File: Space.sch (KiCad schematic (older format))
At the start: 0 parts

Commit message: Replace MCU, route bus
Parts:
- added D66, D67, D68: D_Small, Diodes_SMD:D_SOD-123, symbol D_Small
- added SP1, SP7: MX-2.25U, MX_Alps_Hybrid:MX-2.25U-ReversedStabilizers, symbol MX-2.25U
- added SP2: MX-7U, MX_Alps_Hybrid:MX-7U-ReversedStabilizers, symbol MX-7U
- added SP3: MX-6.25U, MX_Alps_Hybrid:MX-6.25U-ReversedStabilizers, symbol MX-7U
- added SP4: MX-1.25U, MX_Alps_Hybrid:MX-1.25U, symbol MX-7U
- added SP5, SP9: MX-2.75U, MX_Alps_Hybrid:MX-2.75U-ReversedStabilizers, symbol MX-2.25U
- added SP6: MX-6.5U, MX_Alps_Hybrid:MX-6.5U-ReversedStabilizers, symbol MX-7U
- added SP8: MX-1.5U, MX_Alps_Hybrid:MX-1.5U, symbol MX-7U
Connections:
- new net: D67.2 (A), SP2.2 (ROW)
- new net: D66.2 (A), SP1.2 (ROW)
- new net: D68.2 (A), SP5.2 (ROW)
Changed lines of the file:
@@
 $Descr A4 11693 8268
 encoding utf-8
-Sheet 1 6
+Sheet 5 6
 Title ""
 Date ""
@@
 Comment4 ""
 $EndDescr
+$Comp
+L MX-7U SP2
+U 1 1 5ACDBE00
+P 2225 1550
+F 0 "SP2" H 2225 1675 60  0000 C CNN
+F 1 "MX-7U" H 2225 1600 20  0000 C CNN
+F 2 "MX_Alps_Hybrid:MX-7U-ReversedStabilizers" H 2200 1525 60  0001 C CNN
+F 3 "" H 2200 1525 60  0001 C CNN
+	1    2225 1550
+	1    0    0    -1
+$EndComp
+$Comp
+L MX-2.25U SP1
+U 1 1 5ACDBE1D
+P 1525 1550
+F 0 "SP1" H 1525 1675 60  0000 C CNN
+F 1 "MX-2.25U" H 1525 1600 20  0000 C CNN
+F 2 "MX_Alps_Hybrid:MX-2.25U-ReversedStabilizers" H 1500 1525 60  0001 C CNN
+F 3 "" H 1500 1525 60  0001 C CNN
+	1    1525 1550
+	1    0    0    -1
+$EndComp
+$Comp
+L MX-2.25U SP7
+U 1 1 5ACDBE8E
+P 1525 2250
+F 0 "SP7" H 1525 2375 60  0000 C CNN
+F 1 "MX-2.25U" H 1525 2300 20  0000 C CNN
+F 2 "MX_Alps_Hybrid:MX-2.25U-ReversedStabilizers" H 1500 2225 60  0001 C CNN
+F 3 "" H 1500 2225 60  0001 C CNN
+	1    1525 2250
+	1    0    0    -1
+$EndComp
+$Comp
+L D_Small D66
+U 1 1 5ACDBEFA
+P 1425 1825
+F 0 "D66" H 1375 1905 50  0000 L CNN
+F 1 "D_Small" H 1275 1745 50  0000 L CNN
+F 2 "Diodes_SMD:D_SOD-123" V 1425 1825 50  0001 C CNN
+F 3 "" V 1425 1825 50  0001 C CNN
+	1    1425 1825
+	0    -1   -1   0
+$EndComp
+Wire Wire Line
+	1425 1725 1500 1725
+$Comp
+L D_Small D67
+U 1 1 5ACDC3D9
+P 2125 1825
+F 0 "D67" H 2075 1905 50  0000 L CNN
+F 1 "D_Small" H 1975 1745 50  0000 L CNN
+F 2 "Diodes_SMD:D_SOD-123" V 2125 1825 50  0001 C CNN
+F 3 "" V 2125 1825 50  0001 C CNN
+	1    2125 1825
+	0    -1   -1   0
+$EndComp
+Wire Wire Line
+	2125 1725 2200 1725
+$Comp
+L MX-7U SP4
+U 1 1 5ACDC6A9
+P 2225 2250
+F 0 "SP4" H 2225 2375 60  0000 C CNN
+F 1 "MX-1.25U" H 2225 2300 20  0000 C CNN
+F 2 "MX_Alps_Hybrid:MX-1.25U" H 2200 2225 60  0001 C CNN
+F 3 "" H 2200 2225 60  0001 C CNN
+	1    2225 2250
+	1    0    0    -1
+$EndComp
+$Comp
+L MX-7U SP6
+U 1 1 5ACDCCED
+P 2225 2850
+F 0 "SP6" H 2225 2975 60  0000 C CNN
+F 1 "MX-6.5U" H 2225 2900 20  0000 C CNN
+F 2 "MX_Alps_Hybrid:MX-6.5U-ReversedStabilizers" H 2200 2825 60  0001 C CNN
+F 3 "" H 2200 2825 60  0001 C CNN
+	1    2225 2850
+	1    0    0    -1
+$EndComp
+$Comp
+L MX-7U SP8
+U 1 1 5ACDCFF5
+P 2225 3500
+F 0 "SP8" H 2225 3625 60  0000 C CNN
+F 1 "MX-1.5U" H 2225 3550 20  0000 C CNN
+F 2 "MX_Alps_Hybrid:MX-1.5U" H 2200 3475 60  0001 C CNN
+F 3 "" H 2200 3475 60  0001 C CNN
+	1    2225 3500
+	1    0    0    -1
+$EndComp
+$Comp
+L MX-2.25U SP5
+U 1 1 5ACDD407
+P 2900 1550
+F 0 "SP5" H 2900 1675 60  0000 C CNN
+F 1 "MX-2.75U" H 2900 1600 20  0000 C CNN
+F 2 "MX_Alps_Hybrid:MX-2.75U-ReversedStabilizers" H 2875 1525 60  0001 C CNN
+F 3 "" H 2875 1525 60  0001 C CNN
+	1    2900 1550
+	1    0    0    -1
+$EndComp
+$Comp
+L MX-2.25U SP9
+U 1 1 5ACDD40D
+P 2900 2250
+F 0 "SP9" H 2900 2375 60  0000 C CNN
+F 1 "MX-2.75U" H 2900 2300 20  0000 C CNN
+F 2 "MX_Alps_Hybrid:MX-2.75U-ReversedStabilizers" H 2875 2225 60  0001 C CNN
+F 3 "" H 2875 2225 60  0001 C CNN
+	1    2900 2250
+	1    0    0    -1
+$EndComp
+$Comp
+L D_Small D68
+U 1 1 5ACDD413
+P 2800 1825
+F 0 "D68" H 2750 1905 50  0000 L CNN
+F 1 "D_Small" H 2650 1745 50  0000 L CNN
+F 2 "Diodes_SMD:D_SOD-123" V 2800 1825 50  0001 C CNN
+F 3 "" V 2800 1825 50  0001 C CNN
+	1    2800 1825
+	0    -1   -1   0
+$EndComp
+Wire Wire Line
+	2800 1725 2875 1725
+$Comp
+L MX-7U SP3
+U 1 1 5ACDE3EF
+P 2225 4275
+F 0 "SP3" H 2225 4400 60  0000 C CNN
+F 1 "MX-6.25U" H 2225 4325 20  0000 C CNN
+F 2 "MX_Alps_Hybrid:MX-6.25U-ReversedStabilizers" H 2200 4250 60  0001 C CNN
+F 3 "" H 2200 4250 60  0001 C CNN
+	1    2225 4275
+	1    0    0    -1
+$EndComp
 $EndSCHEMATC

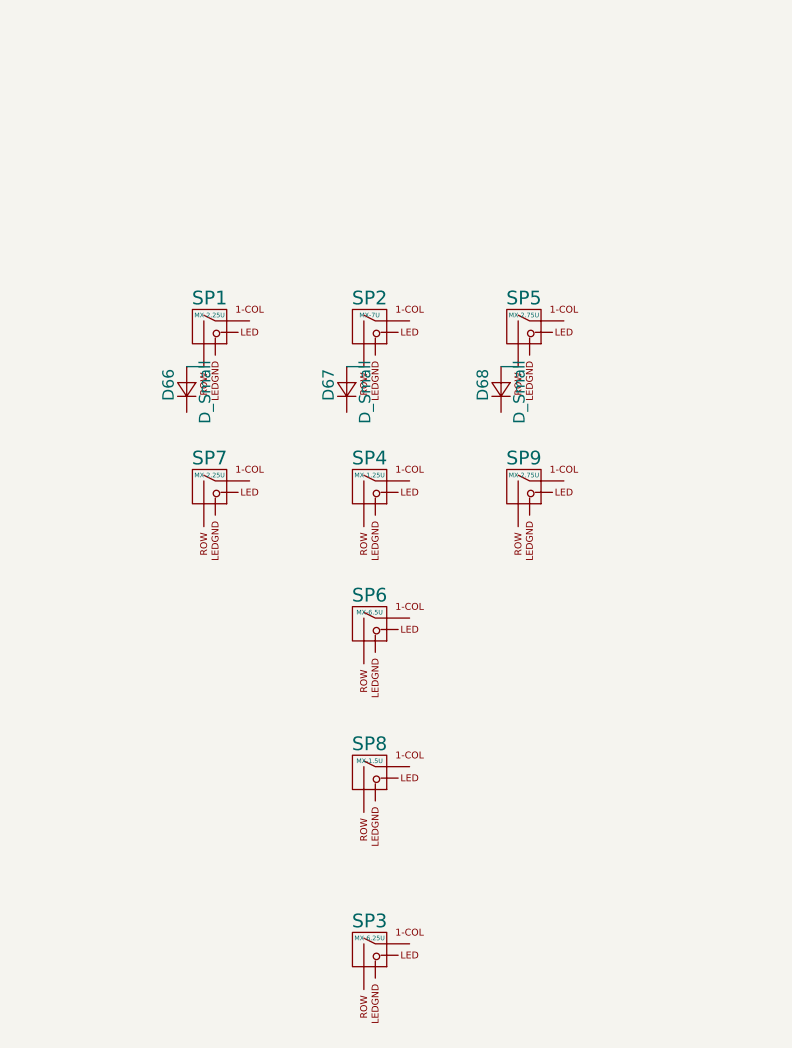
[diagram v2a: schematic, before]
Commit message: Finish project basic routing
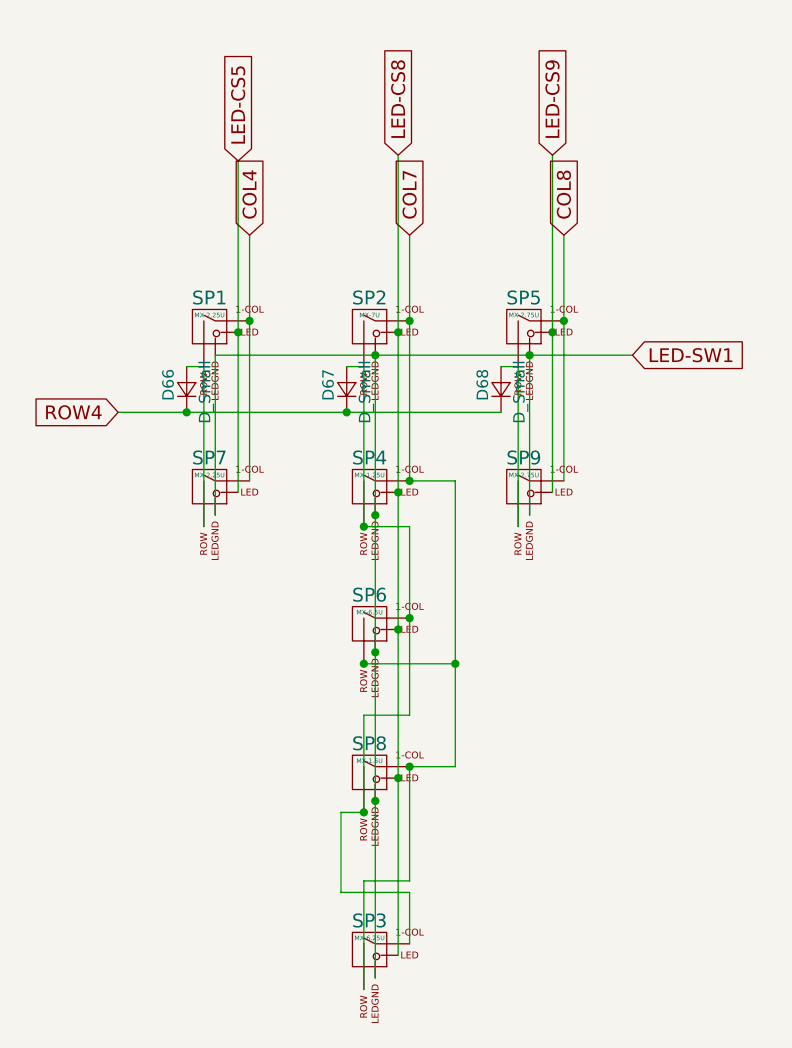
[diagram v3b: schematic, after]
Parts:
- SP4: footprint MX_Alps_Hybrid:MX-1.25U -> MX_Alps_Hybrid:MX-1.25U-FLIPPED
- SP6: footprint MX_Alps_Hybrid:MX-6.5U-ReversedStabilizers -> MX_Alps_Hybrid:MX-6.5U-FLIPPED-ReversedStabilizers
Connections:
- net COL7: now reaches SP2.1 (COL)
- net COL7: now also SP3.2 (ROW), SP4.1 (COL), SP6.2 (ROW), SP8.1 (COL)
- net at D67.2 (A), SP2.2 (ROW): now also SP3.1 (COL), SP4.2 (ROW), SP6.1 (COL), SP8.2 (ROW)
- net LED-CS8: now reaches SP2.3 (LED)
- net LED-CS8: now also SP3.3 (LED), SP4.3 (LED), SP6.3 (LED), SP8.3 (LED)
- net LED-SW1: now reaches SP2.4 (LEDGND)
- net LED-SW1: now also SP1.4 (LEDGND), SP3.4 (LEDGND), SP4.4 (LEDGND), SP5.4 (LEDGND), SP6.4 (LEDGND), SP7.4 (LEDGND), SP8.4 (LEDGND), SP9.4 (LEDGND)
- net COL4: now reaches SP1.1 (COL)
- net COL4: now also SP7.1 (COL)
- net at D66.2 (A), SP1.2 (ROW): now also SP7.2 (ROW)
- net LED-CS5: now reaches SP1.3 (LED)
- net LED-CS5: now also SP7.3 (LED)
- net ROW4: now reaches D66.1 (K)
- net ROW4: now also D67.1 (K), D68.1 (K)
- net COL8: now reaches SP5.1 (COL)
- net COL8: now also SP9.1 (COL)
- net at D68.2 (A), SP5.2 (ROW): now also SP9.2 (ROW)
- net LED-CS9: now reaches SP5.3 (LED)
- net LED-CS9: now also SP9.3 (LED)
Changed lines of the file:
@@
 F 0 "SP4" H 2225 2375 60  0000 C CNN
 F 1 "MX-1.25U" H 2225 2300 20  0000 C CNN
-F 2 "MX_Alps_Hybrid:MX-1.25U" H 2200 2225 60  0001 C CNN
+F 2 "MX_Alps_Hybrid:MX-1.25U-FLIPPED" H 2200 2225 60  0001 C CNN
 F 3 "" H 2200 2225 60  0001 C CNN
 	1    2225 2250
@@
 F 0 "SP6" H 2225 2975 60  0000 C CNN
 F 1 "MX-6.5U" H 2225 2900 20  0000 C CNN
-F 2 "MX_Alps_Hybrid:MX-6.5U-ReversedStabilizers" H 2200 2825 60  0001 C CNN
+F 2 "MX_Alps_Hybrid:MX-6.5U-FLIPPED-ReversedStabilizers" H 2200 2825 60  0001 C CNN
 F 3 "" H 2200 2825 60  0001 C CNN
 	1    2225 2850
-	1    0    0    -1
-$EndComp
-$Comp
-L MX-7U SP8
-U 1 1 5ACDCFF5
-P 2225 3500
-F 0 "SP8" H 2225 3625 60  0000 C CNN
-F 1 "MX-1.5U" H 2225 3550 20  0000 C CNN
-F 2 "MX_Alps_Hybrid:MX-1.5U" H 2200 3475 60  0001 C CNN
-F 3 "" H 2200 3475 60  0001 C CNN
-	1    2225 3500
 	1    0    0    -1
 $EndComp
@@
 	1    0    0    -1
 $EndComp
+Wire Wire Line
+	1700 1150 1700 2225
+Wire Wire Line
+	1500 1725 1500 2425
+Connection ~ 1700 1525
+Wire Wire Line
+	2400 1150 2400 2225
+Wire Wire Line
+	2400 2425 2400 3250
+Wire Wire Line
+	2400 3475 2400 3975
+Connection ~ 2400 1525
+Connection ~ 2400 2225
+Wire Wire Line
+	2200 1725 2200 2425
+Connection ~ 2200 2425
+Connection ~ 2400 2825
+Connection ~ 2200 3675
+Wire Wire Line
+	3075 1150 3075 2225
+Wire Wire Line
+	2875 1725 2875 2425
+Wire Wire Line
+	1125 1925 2800 1925
+Connection ~ 2125 1925
+Connection ~ 1425 1925
+Text GLabel 1125 1925 0    60   Input ~ 0
+ROW4
+$Comp
+L MX-7U SP8
+U 1 1 5ACDCFF5
+P 2225 3500
+F 0 "SP8" H 2225 3625 60  0000 C CNN
+F 1 "MX-1.5U" H 2225 3550 20  0000 C CNN
+F 2 "MX_Alps_Hybrid:MX-1.5U" H 2200 3475 60  0001 C CNN
+F 3 "" H 2200 3475 60  0001 C CNN
+	1    2225 3500
+	1    0    0    -1
+$EndComp
+Wire Wire Line
+	2400 3975 2200 3975
+Wire Wire Line
+	2200 3975 2200 4450
+Wire Wire Line
+	2400 4250 2400 4025
+Wire Wire Line
+	2400 4025 2100 4025
+Wire Wire Line
+	2100 4025 2100 3675
+Wire Wire Line
+	2100 3675 2200 3675
+Connection ~ 2200 3025
+Connection ~ 2400 3475
+Wire Wire Line
+	2400 2225 2600 2225
+Wire Wire Line
+	2600 2225 2600 3475
+Wire Wire Line
+	2600 3025 2200 3025
+Wire Wire Line
+	2200 2425 2400 2425
+Wire Wire Line
+	2400 3250 2200 3250
+Wire Wire Line
+	2200 3250 2200 3675
+Wire Wire Line
+	2600 3475 2400 3475
+Connection ~ 2600 3025
+Connection ~ 3075 1525
+Text GLabel 3075 1150 1    60   Input ~ 0
+COL8
+Text GLabel 2400 1150 1    60   Input ~ 0
+COL7
+Text GLabel 1700 1150 1    60   Input ~ 0
+COL4
+Wire Wire Line
+	1650 825  1650 2275
+Connection ~ 1650 1575
+Text GLabel 1650 825  1    60   Input ~ 0
+LED-CS5
+Wire Wire Line
+	2350 800  2350 4300
+Connection ~ 2350 2275
+Connection ~ 2350 1575
+Text GLabel 2350 800  1    60   Input ~ 0
+LED-CS8
+Wire Wire Line
+	3025 800  3025 2275
+Connection ~ 3025 1575
+Connection ~ 2350 2875
+Connection ~ 2350 3525
+Wire Wire Line
+	2250 1675 2250 4400
+Connection ~ 2250 3625
+Connection ~ 2250 2975
+Connection ~ 2250 2375
+Wire Wire Line
+	2925 1675 2925 2375
+Wire Wire Line
+	1550 2375 1550 1675
+Text GLabel 3025 800  1    60   Input ~ 0
+LED-CS9
+Wire Wire Line
+	1550 1675 3375 1675
+Connection ~ 2250 1675
+Connection ~ 2925 1675
+Text GLabel 3375 1675 2    60   Input ~ 0
+LED-SW1
 $EndSCHEMATC

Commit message: Low cost edition complete
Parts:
- SP1, SP7: footprint MX_Alps_Hybrid:MX-2.25U-ReversedStabilizers -> MX_Alps_Hybrid:MX-2.25U-ReversedStabilizers-NoLED
- SP2: footprint MX_Alps_Hybrid:MX-7U-ReversedStabilizers -> MX_Alps_Hybrid:MX-7U-ReversedStabilizers-NoLED
- SP3: footprint MX_Alps_Hybrid:MX-6.25U-ReversedStabilizers -> MX_Alps_Hybrid:MX-6.25U-ReversedStabilizers-NoLED
- SP4: footprint MX_Alps_Hybrid:MX-1.25U-FLIPPED -> MX_Alps_Hybrid:MX-1.25U-NoLED
- SP5, SP9: footprint MX_Alps_Hybrid:MX-2.75U-ReversedStabilizers -> MX_Alps_Hybrid:MX-2.75U-ReversedStabilizers-NoLED
- SP6: footprint MX_Alps_Hybrid:MX-6.5U-FLIPPED-ReversedStabilizers -> MX_Alps_Hybrid:MX-6.5U-ReversedStabilizers-NoLED
- SP8: footprint MX_Alps_Hybrid:MX-1.5U -> MX_Alps_Hybrid:MX-1.5U-NoLED
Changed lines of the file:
@@
 F 0 "SP2" H 2225 1675 60  0000 C CNN
 F 1 "MX-7U" H 2225 1600 20  0000 C CNN
-F 2 "MX_Alps_Hybrid:MX-7U-ReversedStabilizers" H 2200 1525 60  0001 C CNN
+F 2 "MX_Alps_Hybrid:MX-7U-ReversedStabilizers-NoLED" H 2200 1525 60  0001 C CNN
 F 3 "" H 2200 1525 60  0001 C CNN
 	1    2225 1550
@@
 F 0 "SP1" H 1525 1675 60  0000 C CNN
 F 1 "MX-2.25U" H 1525 1600 20  0000 C CNN
-F 2 "MX_Alps_Hybrid:MX-2.25U-ReversedStabilizers" H 1500 1525 60  0001 C CNN
+F 2 "MX_Alps_Hybrid:MX-2.25U-ReversedStabilizers-NoLED" H 1500 1525 60  0001 C CNN
 F 3 "" H 1500 1525 60  0001 C CNN
 	1    1525 1550
@@
 F 0 "SP7" H 1525 2375 60  0000 C CNN
 F 1 "MX-2.25U" H 1525 2300 20  0000 C CNN
-F 2 "MX_Alps_Hybrid:MX-2.25U-ReversedStabilizers" H 1500 2225 60  0001 C CNN
+F 2 "MX_Alps_Hybrid:MX-2.25U-ReversedStabilizers-NoLED" H 1500 2225 60  0001 C CNN
 F 3 "" H 1500 2225 60  0001 C CNN
 	1    1525 2250
@@
 F 0 "SP4" H 2225 2375 60  0000 C CNN
 F 1 "MX-1.25U" H 2225 2300 20  0000 C CNN
-F 2 "MX_Alps_Hybrid:MX-1.25U-FLIPPED" H 2200 2225 60  0001 C CNN
+F 2 "MX_Alps_Hybrid:MX-1.25U-NoLED" H 2200 2225 60  0001 C CNN
 F 3 "" H 2200 2225 60  0001 C CNN
 	1    2225 2250
@@
 F 0 "SP6" H 2225 2975 60  0000 C CNN
 F 1 "MX-6.5U" H 2225 2900 20  0000 C CNN
-F 2 "MX_Alps_Hybrid:MX-6.5U-FLIPPED-ReversedStabilizers" H 2200 2825 60  0001 C CNN
+F 2 "MX_Alps_Hybrid:MX-6.5U-ReversedStabilizers-NoLED" H 2200 2825 60  0001 C CNN
 F 3 "" H 2200 2825 60  0001 C CNN
 	1    2225 2850
@@
 F 0 "SP5" H 2900 1675 60  0000 C CNN
 F 1 "MX-2.75U" H 2900 1600 20  0000 C CNN
-F 2 "MX_Alps_Hybrid:MX-2.75U-ReversedStabilizers" H 2875 1525 60  0001 C CNN
+F 2 "MX_Alps_Hybrid:MX-2.75U-ReversedStabilizers-NoLED" H 2875 1525 60  0001 C CNN
 F 3 "" H 2875 1525 60  0001 C CNN
 	1    2900 1550
@@
 F 0 "SP9" H 2900 2375 60  0000 C CNN
 F 1 "MX-2.75U" H 2900 2300 20  0000 C CNN
-F 2 "MX_Alps_Hybrid:MX-2.75U-ReversedStabilizers" H 2875 2225 60  0001 C CNN
+F 2 "MX_Alps_Hybrid:MX-2.75U-ReversedStabilizers-NoLED" H 2875 2225 60  0001 C CNN
 F 3 "" H 2875 2225 60  0001 C CNN
 	1    2900 2250
@@
 F 0 "SP3" H 2225 4400 60  0000 C CNN
 F 1 "MX-6.25U" H 2225 4325 20  0000 C CNN
-F 2 "MX_Alps_Hybrid:MX-6.25U-ReversedStabilizers" H 2200 4250 60  0001 C CNN
+F 2 "MX_Alps_Hybrid:MX-6.25U-ReversedStabilizers-NoLED" H 2200 4250 60  0001 C CNN
 F 3 "" H 2200 4250 60  0001 C CNN
 	1    2225 4275
@@
 F 0 "SP8" H 2225 3625 60  0000 C CNN
 F 1 "MX-1.5U" H 2225 3550 20  0000 C CNN
-F 2 "MX_Alps_Hybrid:MX-1.5U" H 2200 3475 60  0001 C CNN
+F 2 "MX_Alps_Hybrid:MX-1.5U-NoLED" H 2200 3475 60  0001 C CNN
 F 3 "" H 2200 3475 60  0001 C CNN
 	1    2225 3500
